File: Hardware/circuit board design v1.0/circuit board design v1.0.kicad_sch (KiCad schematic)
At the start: 0 parts

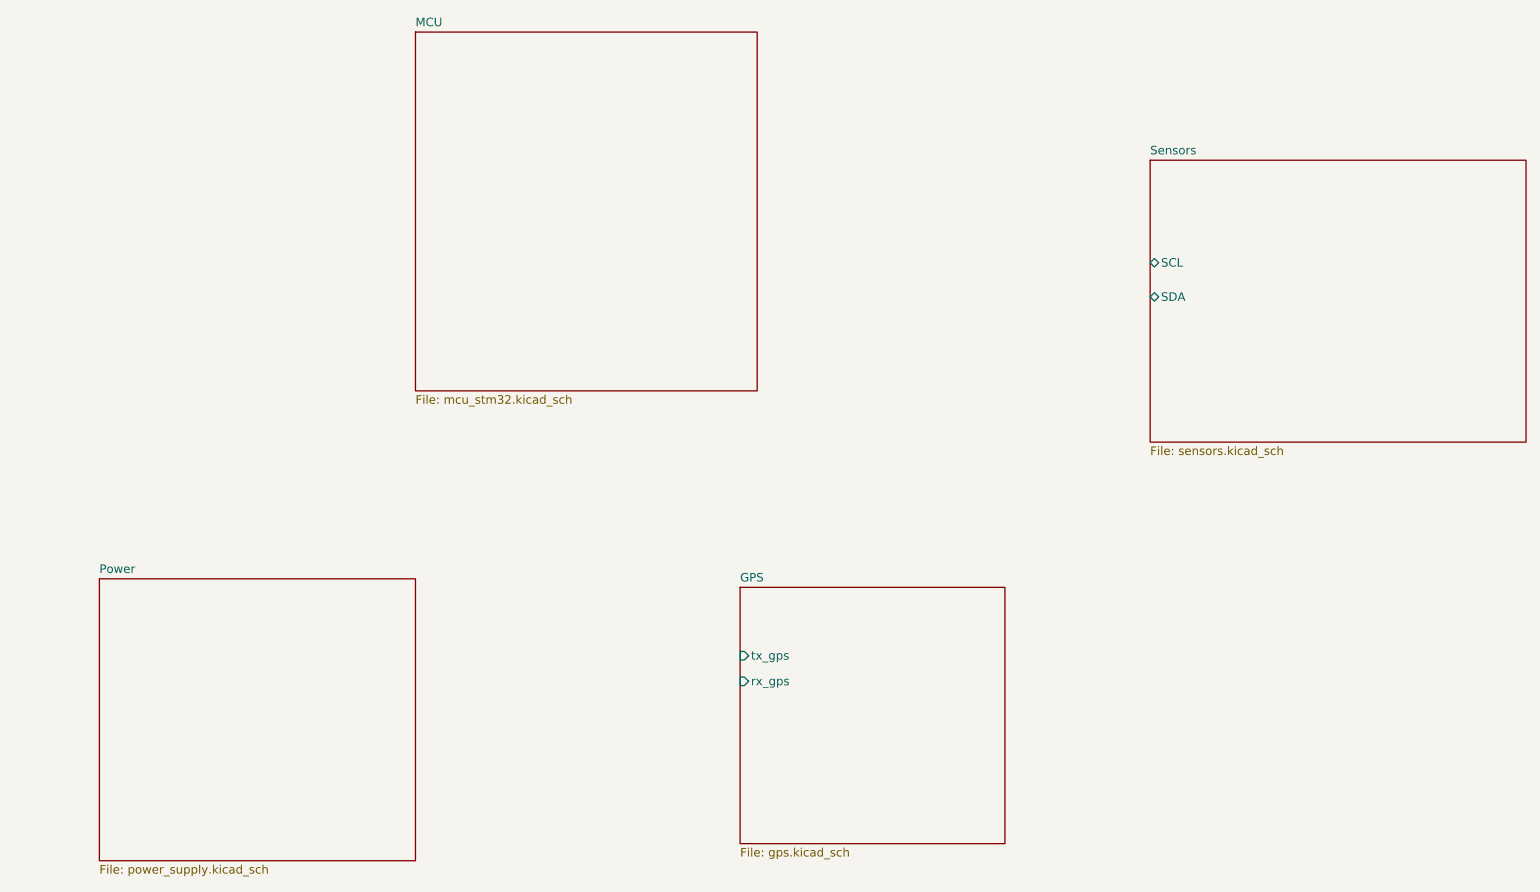
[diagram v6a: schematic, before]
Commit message: Created stm32mx project and started on layout
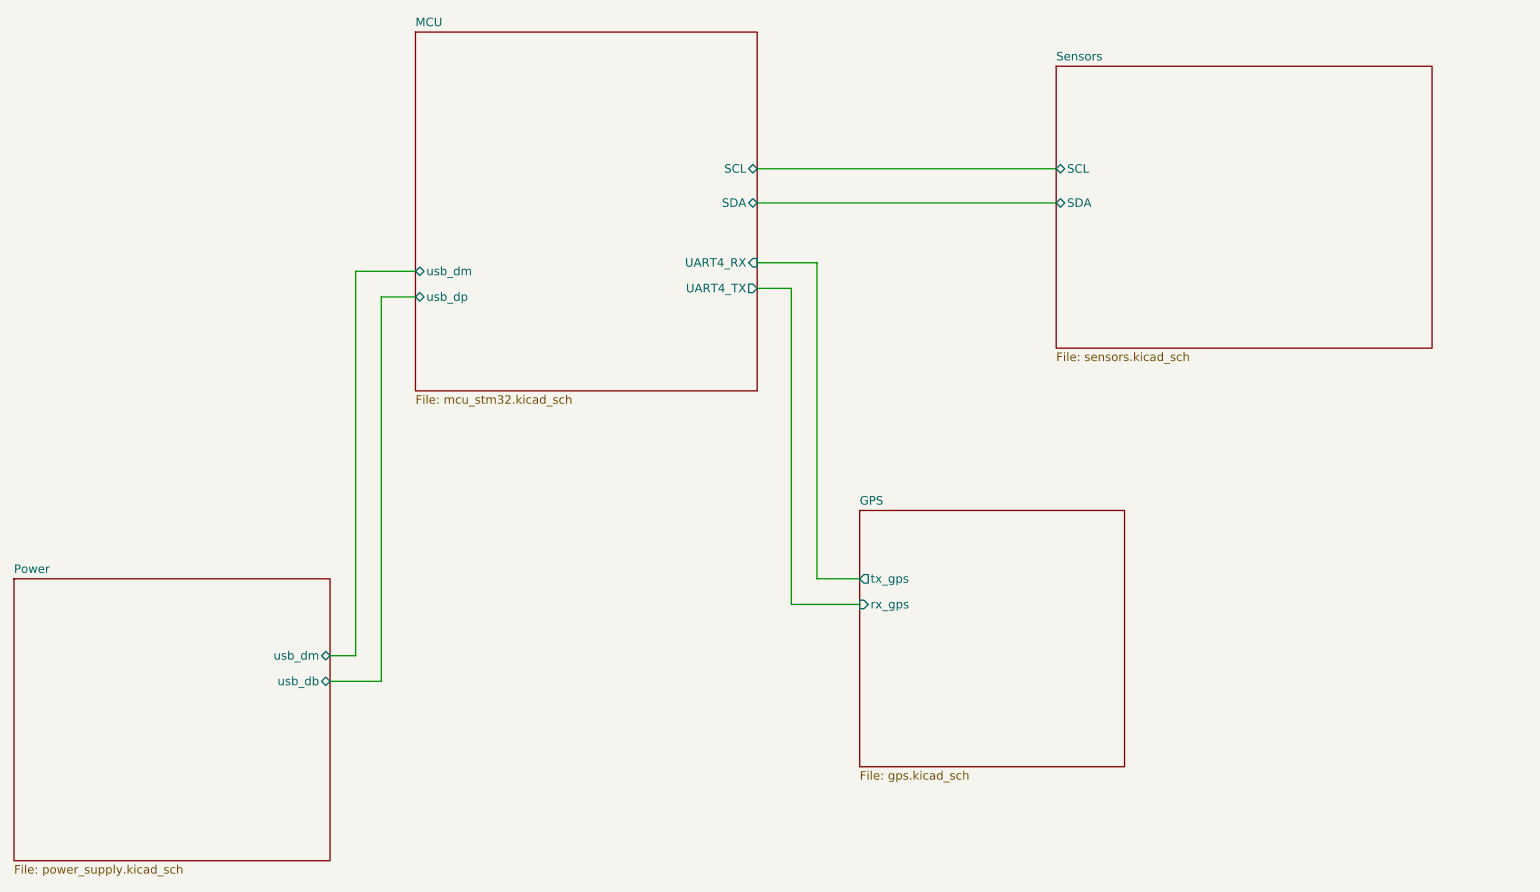
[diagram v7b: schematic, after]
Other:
- sheet MCU ports: added SCL, SDA, UART4_RX, UART4_TX, usb_dm, usb_dp; removed none
- sheet Power ports: added usb_db, usb_dm; removed none
